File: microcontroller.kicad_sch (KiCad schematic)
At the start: 23 parts, among them J11 VOX_IN, J12 VOX_TRX, J6 I2C, J7 SW1_CON, J8 I2C, SW1 SW_Push, U3 ESP32-DEVKIT

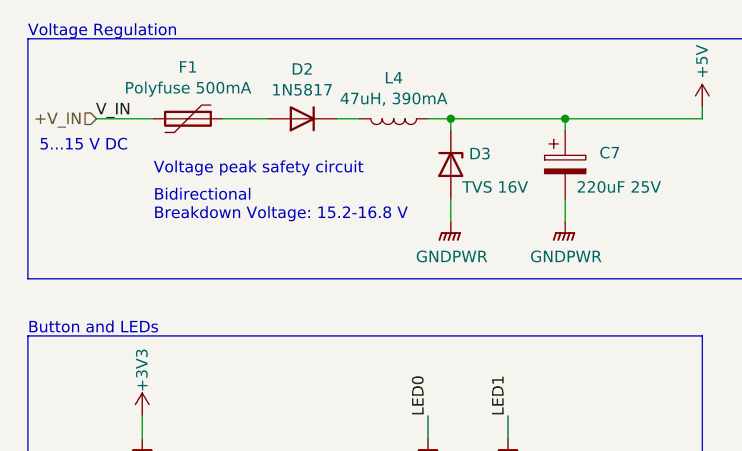
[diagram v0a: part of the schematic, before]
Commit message: am: fixed #30 Suboptimal placement of D3
* Swapped D3 and L4 according to Issue #30
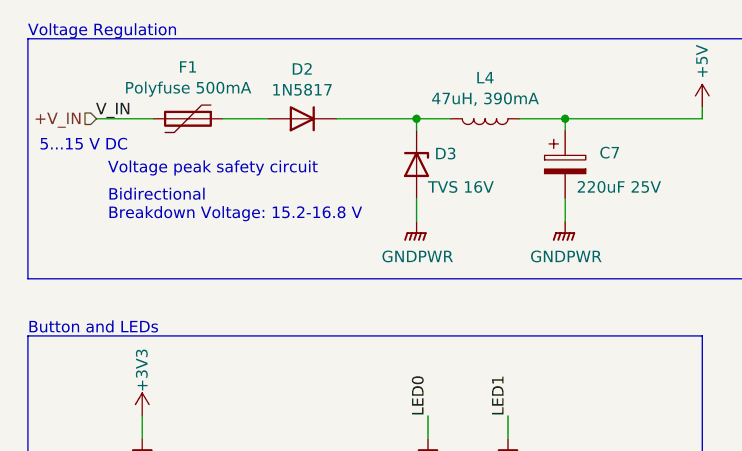
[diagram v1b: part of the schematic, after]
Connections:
- net +5V: no longer D3.1 (K)
- net at D2.1 (K), L4.2: now also D3.1 (K)
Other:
- moved on the sheet: D3, L4
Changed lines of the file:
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@@
   (junction (at 24.13 72.39) (diameter 0) (color 0 0 0 0)
   )
-  (junction (at 64.77 26.67) (diameter 0) (color 0 0 0 0)
+  (junction (at 77.47 26.67) (diameter 0) (color 0 0 0 0)
   )
   (junction (at 73.66 120.65) (diameter 0) (color 0 0 0 0)
   )
-  (junction (at 77.47 26.67) (diameter 0) (color 0 0 0 0)
+  (junction (at 60.96 26.67) (diameter 0) (color 0 0 0 0)
   )
   (no_connect (at 175.26 40.64))
@@
     (stroke (width 0) (type default) (color 0 0 0 0))
   )
+  (wire (pts (xy 64.77 26.67) (xy 60.96 26.67))
+    (stroke (width 0) (type default) (color 0 0 0 0))
+  )
   (wire (pts (xy 215.9 33.02) (xy 218.44 33.02))
     (stroke (width 0) (type default) (color 0 0 0 0))
@@
     (stroke (width 0) (type default) (color 0 0 0 0))
   )
-  (wire (pts (xy 64.77 27.94) (xy 64.77 26.67))
-    (stroke (width 0) (type default) (color 0 0 0 0))
-  )
   (wire (pts (xy 71.12 62.23) (xy 71.12 59.69))
     (stroke (width 0) (type default) (color 0 0 0 0))
@@
     (stroke (width 0) (type default) (color 0 0 0 0))
   )
-  (wire (pts (xy 64.77 35.56) (xy 64.77 38.1))
+  (wire (pts (xy 60.96 35.56) (xy 60.96 38.1))
     (stroke (width 0) (type default) (color 0 0 0 0))
   )
@@
     (stroke (width 0) (type default) (color 0 0 0 0))
   )
-  (wire (pts (xy 52.07 26.67) (xy 54.61 26.67))
+  (wire (pts (xy 72.39 26.67) (xy 77.47 26.67))
+    (stroke (width 0) (type default) (color 0 0 0 0))
+  )
+  (wire (pts (xy 52.07 26.67) (xy 60.96 26.67))
     (stroke (width 0) (type default) (color 0 0 0 0))
   )
@@
     (stroke (width 0) (type default) (color 0 0 0 0))
   )
+  (wire (pts (xy 60.96 26.67) (xy 60.96 27.94))
+    (stroke (width 0) (type default) (color 0 0 0 0))
+  )
   (wire (pts (xy 71.12 69.85) (xy 71.12 73.66))
     (stroke (width 0) (type default) (color 0 0 0 0))
@@
     (stroke (width 0) (type default) (color 0 0 0 0))
   )
-  (wire (pts (xy 64.77 26.67) (xy 77.47 26.67))
-    (stroke (width 0) (type default) (color 0 0 0 0))
-  )
   (wire (pts (xy 171.45 58.42) (xy 175.26 58.42))
     (stroke (width 0) (type default) (color 0 0 0 0))
@@
     (stroke (width 0) (type default) (color 0 0 0 0))
   )
-  (wire (pts (xy 62.23 26.67) (xy 64.77 26.67))
-    (stroke (width 0) (type default) (color 0 0 0 0))
-  )
   (wire (pts (xy 36.83 72.39) (xy 30.48 72.39))
     (stroke (width 0) (type default) (color 0 0 0 0))
@@
     (effects (font (size 1.27 1.27)) (justify left bottom))
   )
-  (text "Voltage peak safety circuit" (at 31.75 33.02 0)
+  (text "Voltage peak safety circuit" (at 26.67 33.02 0)
     (effects (font (size 1.27 1.27)) (justify left bottom))
   )
@@
     (effects (font (size 1.27 1.27)) (justify right bottom))
   )
-  (text "Bidirectional\nBreakdown Voltage: 15.2-16.8 V" (at 31.75 38.1 0)
+  (text "Bidirectional\nBreakdown Voltage: 15.2-16.8 V" (at 26.67 38.1 0)
     (effects (font (size 1.27 1.27)) (justify left bottom))
   )
@@
     (pin "2")
   )
-  (symbol (lib_id "Device:L") (at 58.42 26.67 270) (unit 1)
-    (in_bom yes) (on_board yes)
-    (property "Reference" "L4" (id 0) (at 58.42 22.1488 90))
-    (property "Value" "47uH, 390mA" (id 1) (at 58.42 24.4602 90))
-    (property "Footprint" "Inductor_SMD:L_Wuerth_MAPI-3020" (id 2) (at 58.42 26.67 0)
-      (effects (font (size 1.27 1.27)) hide)
-    )
-    (property "Datasheet" "~" (id 3) (at 58.42 26.67 0)
-      (effects (font (size 1.27 1.27)) hide)
-    )
-    (property "Mouser Best.Nr." "710-74438335470" (id 4) (at 58.42 26.67 90)
-      (effects (font (size 1.27 1.27)) hide)
-    )
-    (property "PartNrDigikey" "732-4872-1-ND" (id 5) (at 58.42 26.67 0)
-      (effects (font (size 1.27 1.27)) hide)
-    )
-    (pin "1")
-    (pin "2")
-  )
-  (symbol (lib_id "Device:D_Zener") (at 64.77 31.75 270) (unit 1)
-    (in_bom yes) (on_board yes)
-    (property "Reference" "D3" (id 0) (at 66.7766 30.5816 90)
-      (effects (font (size 1.27 1.27)) (justify left))
-    )
-    (property "Value" "TVS 16V" (id 1) (at 66.04 34.29 90)
-      (effects (font (size 1.27 1.27)) (justify left))
-    )
-    (property "Footprint" "Diode_SMD:D_SMB" (id 2) (at 64.77 31.75 0)
-      (effects (font (size 1.27 1.27)) hide)
-    )
-    (property "Datasheet" "~" (id 3) (at 64.77 31.75 0)
-      (effects (font (size 1.27 1.27)) hide)
-    )
-    (property "Mouser Best.Nr." "652-P6SMB16CA" (id 4) (at 64.77 31.75 90)
-      (effects (font (size 1.27 1.27)) hide)
-    )
-    (property "PartNrDigikey" "P6SMB16CABBCT-ND" (id 5) (at 64.77 31.75 0)
+  (symbol (lib_id "Device:L") (at 68.58 26.67 270) (unit 1)
+    (in_bom yes) (on_board yes)
+    (property "Reference" "L4" (id 0) (at 68.58 22.1488 90))
+    (property "Value" "47uH, 390mA" (id 1) (at 68.58 24.4602 90))
+    (property "Footprint" "Inductor_SMD:L_Wuerth_MAPI-3020" (id 2) (at 68.58 26.67 0)
+      (effects (font (size 1.27 1.27)) hide)
+    )
+    (property "Datasheet" "~" (id 3) (at 68.58 26.67 0)
+      (effects (font (size 1.27 1.27)) hide)
+    )
+    (property "Mouser Best.Nr." "710-74438335470" (id 4) (at 68.58 26.67 90)
+      (effects (font (size 1.27 1.27)) hide)
+    )
+    (property "PartNrDigikey" "732-4872-1-ND" (id 5) (at 68.58 26.67 0)
+      (effects (font (size 1.27 1.27)) hide)
+    )
+    (pin "1")
+    (pin "2")
+  )
+  (symbol (lib_id "Device:D_Zener") (at 60.96 31.75 270) (unit 1)
+    (in_bom yes) (on_board yes)
+    (property "Reference" "D3" (id 0) (at 62.9666 30.5816 90)
+      (effects (font (size 1.27 1.27)) (justify left))
+    )
+    (property "Value" "TVS 16V" (id 1) (at 62.23 34.29 90)
+      (effects (font (size 1.27 1.27)) (justify left))
+    )
+    (property "Footprint" "Diode_SMD:D_SMB" (id 2) (at 60.96 31.75 0)
+      (effects (font (size 1.27 1.27)) hide)
+    )
+    (property "Datasheet" "~" (id 3) (at 60.96 31.75 0)
+      (effects (font (size 1.27 1.27)) hide)
+    )
+    (property "Mouser Best.Nr." "652-P6SMB16CA" (id 4) (at 60.96 31.75 90)
+      (effects (font (size 1.27 1.27)) hide)
+    )
+    (property "PartNrDigikey" "P6SMB16CABBCT-ND" (id 5) (at 60.96 31.75 0)
       (effects (font (size 1.27 1.27)) hide)
     )
@@
     (pin "1")
   )
-  (symbol (lib_id "power:GNDPWR") (at 64.77 38.1 0) (unit 1)
-    (in_bom yes) (on_board yes)
-    (property "Reference" "#PWR027" (id 0) (at 64.77 43.18 0)
-      (effects (font (size 1.27 1.27)) hide)
-    )
-    (property "Value" "GNDPWR" (id 1) (at 64.8716 42.0116 0))
-    (property "Footprint" "" (id 2) (at 64.77 39.37 0)
-      (effects (font (size 1.27 1.27)) hide)
-    )
-    (property "Datasheet" "" (id 3) (at 64.77 39.37 0)
-      (effects (font (size 1.27 1.27)) hide)
-    )
+  (symbol (lib_id "power:GNDPWR") (at 60.96 38.1 0) (unit 1)
+    (in_bom yes) (on_board yes)
+    (property "Reference" "#PWR027" (id 0) (at 60.96 43.18 0)
+      (effects (font (size 1.27 1.27)) hide)
+    )
+    (property "Value" "GNDPWR" (id 1) (at 61.0616 42.0116 0))
+    (property "Footprint" "" (id 2) (at 60.96 39.37 0)
+      (effects (font (size 1.27 1.27)) hide)
+    )
+    (property "Datasheet" "" (id 3) (at 60.96 39.37 0)
+      (effects (font (size 1.27 1.27)) hide)
+    )
